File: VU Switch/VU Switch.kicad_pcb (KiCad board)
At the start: 2 copper layers, 99.1 x 71.8 mm, 31 parts, among them J1 DC_12V, J10 VU_12V, J11 LED, J12 VU_5V, J13 VU_12V, J2 VU_12V, J3 SELECT, J4 INPUT1, J5 INPUT2, J6 INPUT3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

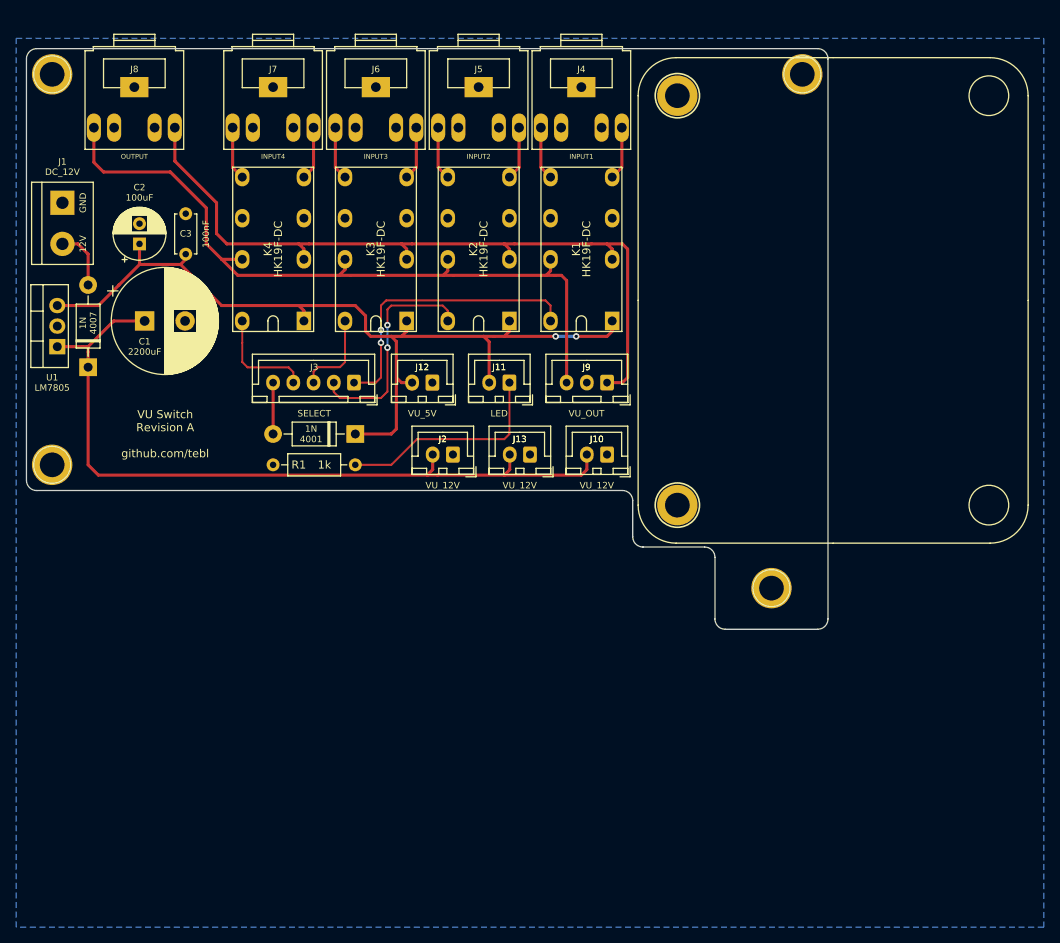
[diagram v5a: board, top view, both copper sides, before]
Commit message: Tweaked audio jack position, changed power connector to XH.
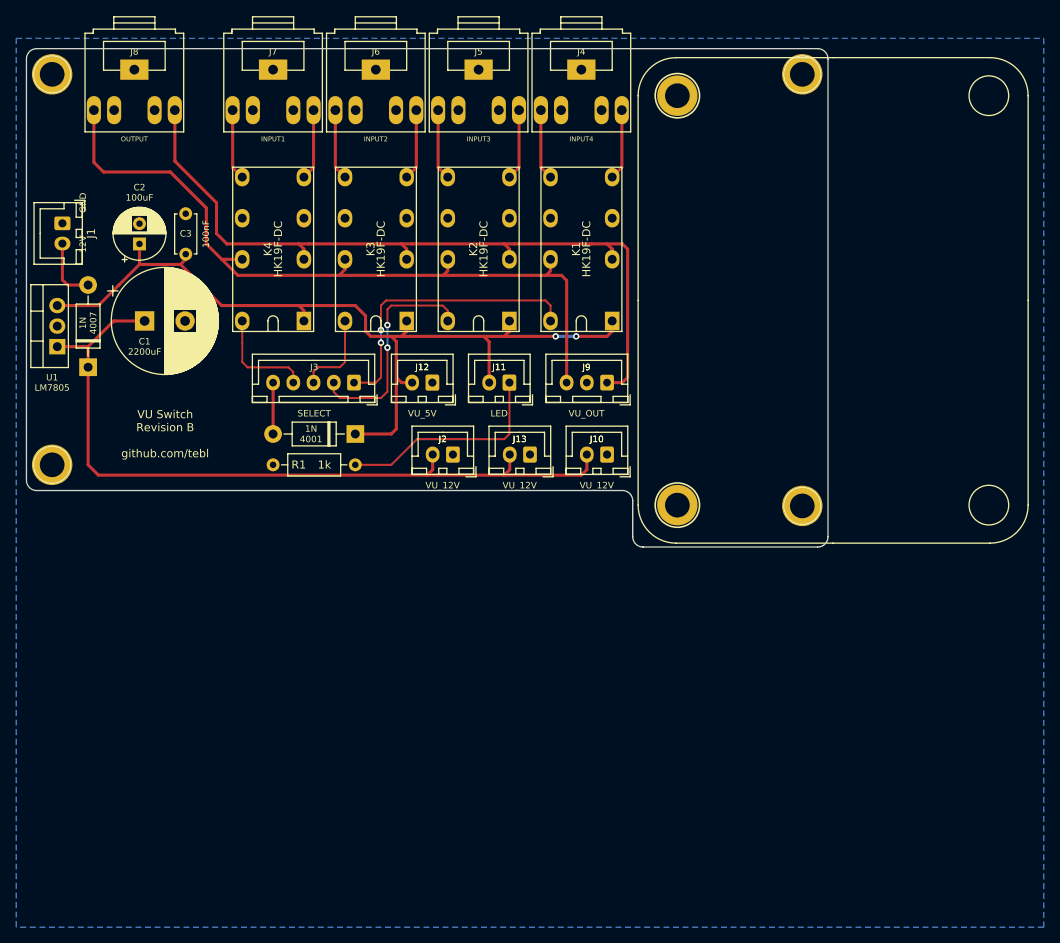
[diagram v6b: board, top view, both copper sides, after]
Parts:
- J1: footprint TerminalBlock:TerminalBlock_bornier-2_P5.08mm -> Connector_JST:JST_XH_B2B-XH-A_1x02_P2.50mm_Vertical
- J4: value INPUT1 -> INPUT4
- J5: value INPUT2 -> INPUT3
- J6: value INPUT3 -> INPUT2
- J7: value INPUT4 -> INPUT1
- moved M2 10.9 mm to (184.8, 106.7)
- moved J1 2.54 mm to (93.3, 71.8)
- moved J4 2.16 mm to (157.5, 54.4)
- moved J5 2.16 mm to (144.8, 54.4)
- moved J6 2.16 mm to (132.1, 54.4)
- moved J7 2.16 mm to (119.4, 54.4)
- moved J8 2.16 mm to (102.2, 54.4)
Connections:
- J3 pad 1: SELECT_1 -> SELECT_4
- J3 pad 2: SELECT_2 -> SELECT_3
- J3 pad 3: SELECT_3 -> SELECT_2
- J3 pad 4: SELECT_4 -> SELECT_1
- K1 pad 16: SELECT_1 -> SELECT_4
- K2 pad 16: SELECT_2 -> SELECT_3
- K3 pad 16: SELECT_3 -> SELECT_2
- K4 pad 16: SELECT_4 -> SELECT_1
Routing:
- net SELECT_4: track 13.2 -> 35.9 mm, vias 0 -> 2
- net SELECT_1: track 35.9 -> 13.2 mm, vias 2 -> 0
- net SELECT_3: track 10.8 -> 27.8 mm, vias 0 -> 2
- net SELECT_2: track 27.8 -> 10.8 mm, vias 2 -> 0
- net OUT_L: track 93.2 -> 95.4 mm
- net Net-(J6-Pad5): track 6.61 -> 8.77 mm
- net Net-(J6-Pad2): track 6.61 -> 8.77 mm
- net Net-(J7-Pad5): track 6.61 -> 8.77 mm
- net Net-(J7-Pad2): track 6.61 -> 8.77 mm
- net Net-(J5-Pad5): track 6.61 -> 8.77 mm
- net Net-(J5-Pad2): track 6.61 -> 8.77 mm
- net Net-(J4-Pad5): track 6.61 -> 8.77 mm
- net Net-(J4-Pad2): track 6.61 -> 8.77 mm
- net OUT_R: track 94.2 -> 96.3 mm
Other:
- board size 99.1 x 71.8 mm -> 99.1 x 61.6 mm
- board text added: "VU Switch Revision B github.com/tebl"
- board text removed: "VU Switch Revision A github.com/tebl"

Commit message: Updated gerber files
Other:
- board text added: "12v"
- board text added: "5v"
- board text added: "CH1"
- board text added: "CH2"
- board text added: "CH3"
- board text added: "CH4"
- board text added: "L"
- board text added: "R"
- board text added: "R1"
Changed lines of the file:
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@@
   (general
     (thickness 1.6)
-    (drawings 27)
+    (drawings 45)
     (tracks 170)
     (zones 0)
@@
     (descr "JST XH series connector, B2B-XH-A (http://www.jst-mfg.com/product/pdf/eng/eXH.pdf), generated with kicad-footprint-generator")
     (tags "connector JST XH vertical")
-    (fp_text reference J1 (at 1.25 -3.55 90) (layer F.SilkS)
-      (effects (font (size 1 1) (thickness 0.15)))
-    )
-    (fp_text value DC_12V (at 1.25 4.6 90) (layer F.Fab)
-      (effects (font (size 1 1) (thickness 0.15)))
+    (fp_text reference J1 (at -5.08 1.27 180) (layer F.SilkS)
+      (effects (font (size 0.8 0.8) (thickness 0.1)))
+    )
+    (fp_text value DC_12V (at -3.81 1.27 180) (layer F.SilkS)
+      (effects (font (size 0.8 0.8) (thickness 0.1)))
     )
     (fp_line (start -2.85 -2.75) (end -2.85 -1.5) (layer F.SilkS) (width 0.12))
@@
     )
   )
+  (gr_text CH4 (at 129.54 93.345) (layer B.SilkS)
+    (effects (font (size 0.8 0.8) (thickness 0.1)) (justify mirror))
+  )
+  (gr_text CH3 (at 127 89.535) (layer B.SilkS)
+    (effects (font (size 0.8 0.8) (thickness 0.1)) (justify mirror))
+  )
+  (gr_text CH2 (at 124.46 93.345) (layer B.SilkS)
+    (effects (font (size 0.8 0.8) (thickness 0.1)) (justify mirror))
+  )
+  (gr_text CH1 (at 121.92 89.535) (layer B.SilkS)
+    (effects (font (size 0.8 0.8) (thickness 0.1)) (justify mirror))
+  )
+  (gr_text GND (at 119.38 93.345) (layer B.SilkS)
+    (effects (font (size 0.8 0.8) (thickness 0.1)) (justify mirror))
+  )
+  (gr_text R1 (at 148.59 93.345) (layer B.SilkS)
+    (effects (font (size 0.8 0.8) (thickness 0.1)) (justify mirror))
+  )
+  (gr_text GND (at 139.065 93.345) (layer B.SilkS)
+    (effects (font (size 0.8 0.8) (thickness 0.1)) (justify mirror))
+  )
+  (gr_text GND (at 158.115 93.345) (layer B.SilkS)
+    (effects (font (size 0.8 0.8) (thickness 0.1)) (justify mirror))
+  )
+  (gr_text GND (at 160.655 102.235) (layer B.SilkS)
+    (effects (font (size 0.8 0.8) (thickness 0.1)) (justify mirror))
+  )
+  (gr_text GND (at 151.13 102.235) (layer B.SilkS)
+    (effects (font (size 0.8 0.8) (thickness 0.1)) (justify mirror))
+  )
+  (gr_text GND (at 141.605 102.235) (layer B.SilkS)
+    (effects (font (size 0.8 0.8) (thickness 0.1)) (justify mirror))
+  )
+  (gr_text 12v (at 158.115 98.425) (layer B.SilkS)
+    (effects (font (size 0.8 0.8) (thickness 0.1)) (justify mirror))
+  )
+  (gr_text 12v (at 139.065 98.425) (layer B.SilkS)
+    (effects (font (size 0.8 0.8) (thickness 0.1)) (justify mirror))
+  )
+  (gr_text 12v (at 148.59 98.425) (layer B.SilkS)
+    (effects (font (size 0.8 0.8) (thickness 0.1)) (justify mirror))
+  )
+  (gr_text 5v (at 136.525 89.535) (layer B.SilkS)
+    (effects (font (size 0.8 0.8) (thickness 0.1)) (justify mirror))
+  )
+  (gr_text 5v (at 146.05 89.535) (layer B.SilkS)
+    (effects (font (size 0.8 0.8) (thickness 0.1)) (justify mirror))
+  )
+  (gr_text R (at 160.655 89.535) (layer B.SilkS)
+    (effects (font (size 0.8 0.8) (thickness 0.1)) (justify mirror))
+  )
+  (gr_text L (at 155.575 89.535) (layer B.SilkS)
+    (effects (font (size 0.8 0.8) (thickness 0.1)) (justify mirror))
+  )
   (gr_circle (center 169.345 55.98) (end 172.085 55.98) (layer F.SilkS) (width 0.2))
   (gr_circle (center 169.345 106.58) (end 172.085 106.58) (layer F.SilkS) (width 0.2))
@@
   (gr_arc (start 162.56 106.045) (end 163.83 106.045) (angle -90) (layer Edge.Cuts) (width 0.05))
   (gr_arc (start 165.1 110.49) (end 163.83 110.49) (angle -90) (layer Edge.Cuts) (width 0.05))
-  (gr_text GND (at 95.885 69.215 90) (layer F.SilkS)
+  (gr_text GND (at 97.155 70.485 90) (layer F.SilkS)
     (effects (font (size 0.8 0.8) (thickness 0.1)))
   )
-  (gr_text 12V (at 95.885 74.295 90) (layer F.SilkS)
+  (gr_text 12V (at 97.155 75.565 90) (layer F.SilkS)
     (effects (font (size 0.8 0.8) (thickness 0.1)))
   )
